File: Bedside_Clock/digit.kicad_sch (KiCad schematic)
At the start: 21 parts

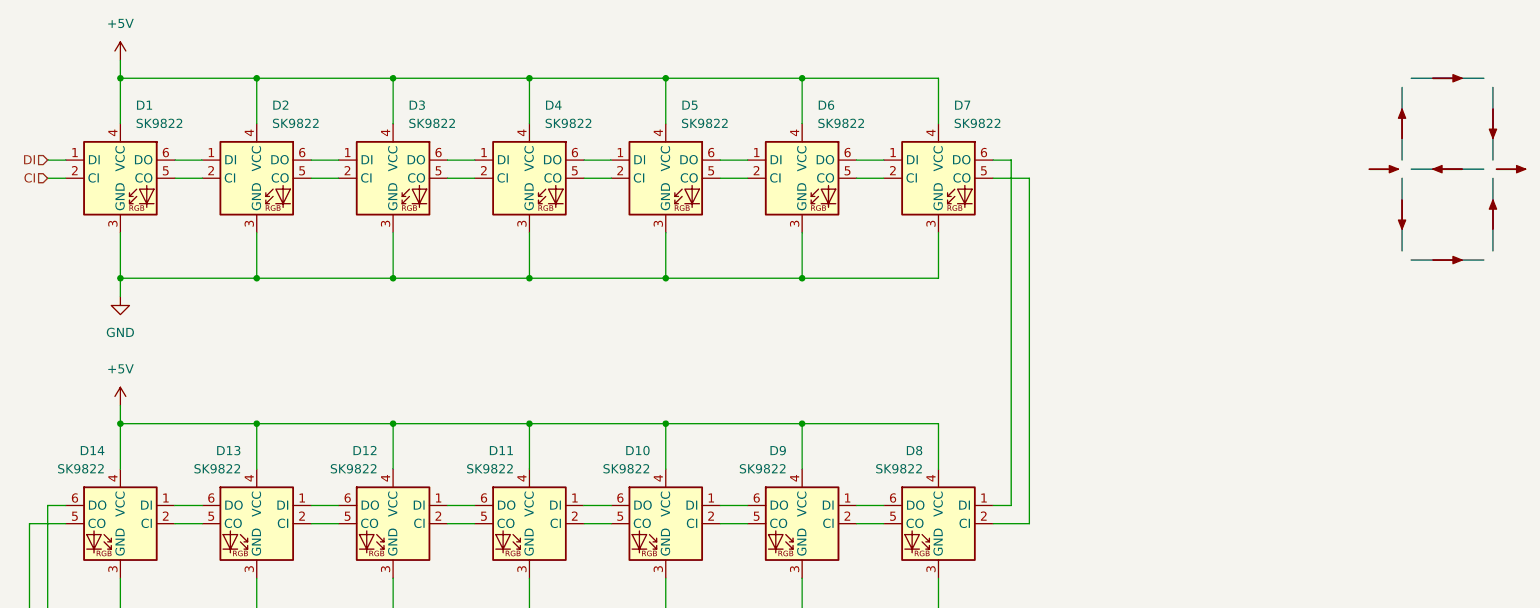
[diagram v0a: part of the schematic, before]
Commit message: [HW] Switch to HD107s (maybe switch to 108s)
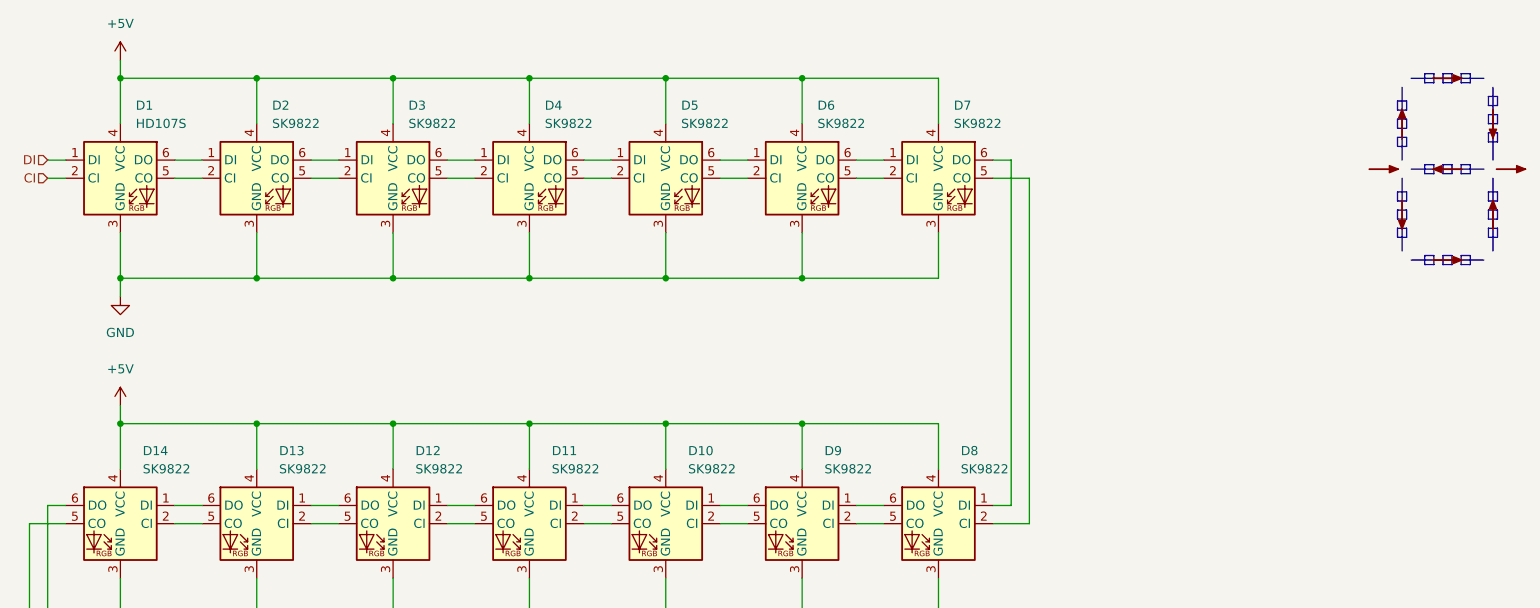
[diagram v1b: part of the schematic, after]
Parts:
- D1: value SK9822 -> HD107S; footprint (none) -> LED_SMD:LED_RGB_5050-6; symbol LED:APA102 -> LED:HD107s; Site (none) -> https://www.ledlightinghut.com/hd107s-5050-rgb-led.html
- D10, D11, D12, D13, D14, D15, D16, D17, D18, D19, D2, D20, D21, D3, D4, D5, D6, D7, D8, D9: footprint (none) -> LED_SMD:LED_RGB_5050-6; symbol LED:APA102 -> LED:HD107s; Site (none) -> https://www.ledlightinghut.com/hd107s-5050-rgb-led.html

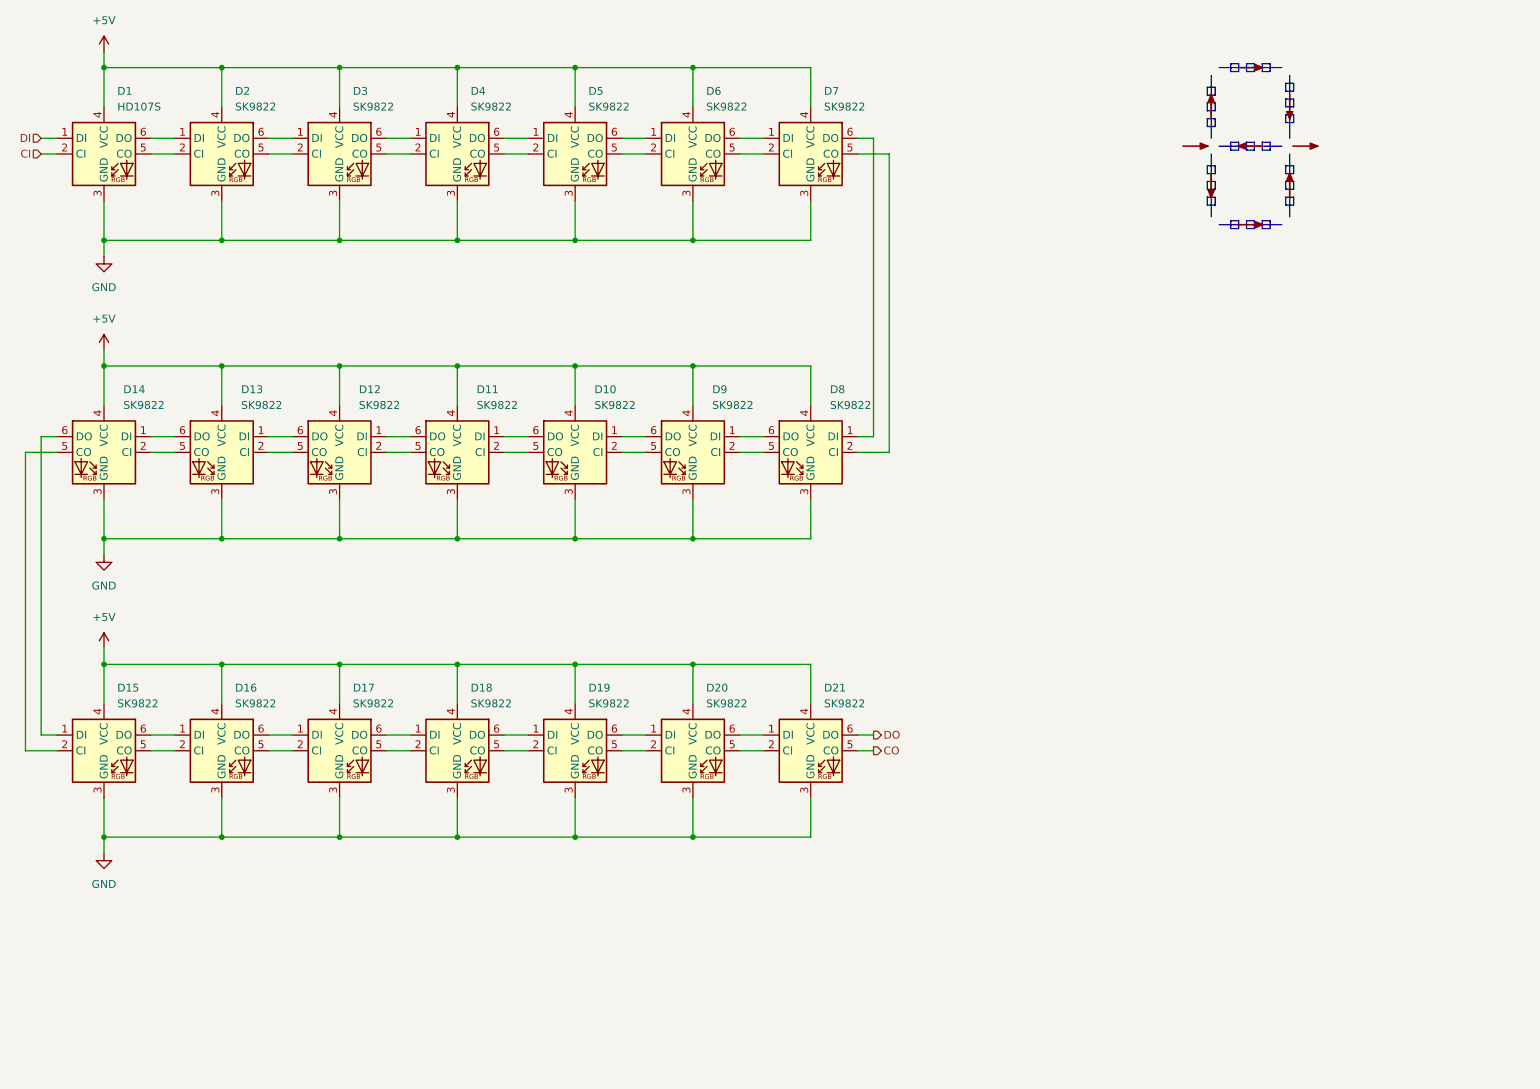
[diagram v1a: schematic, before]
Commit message: [HW] Layout LEDs and first pass add of ESP32 Also add decoupling caps for all LEDs
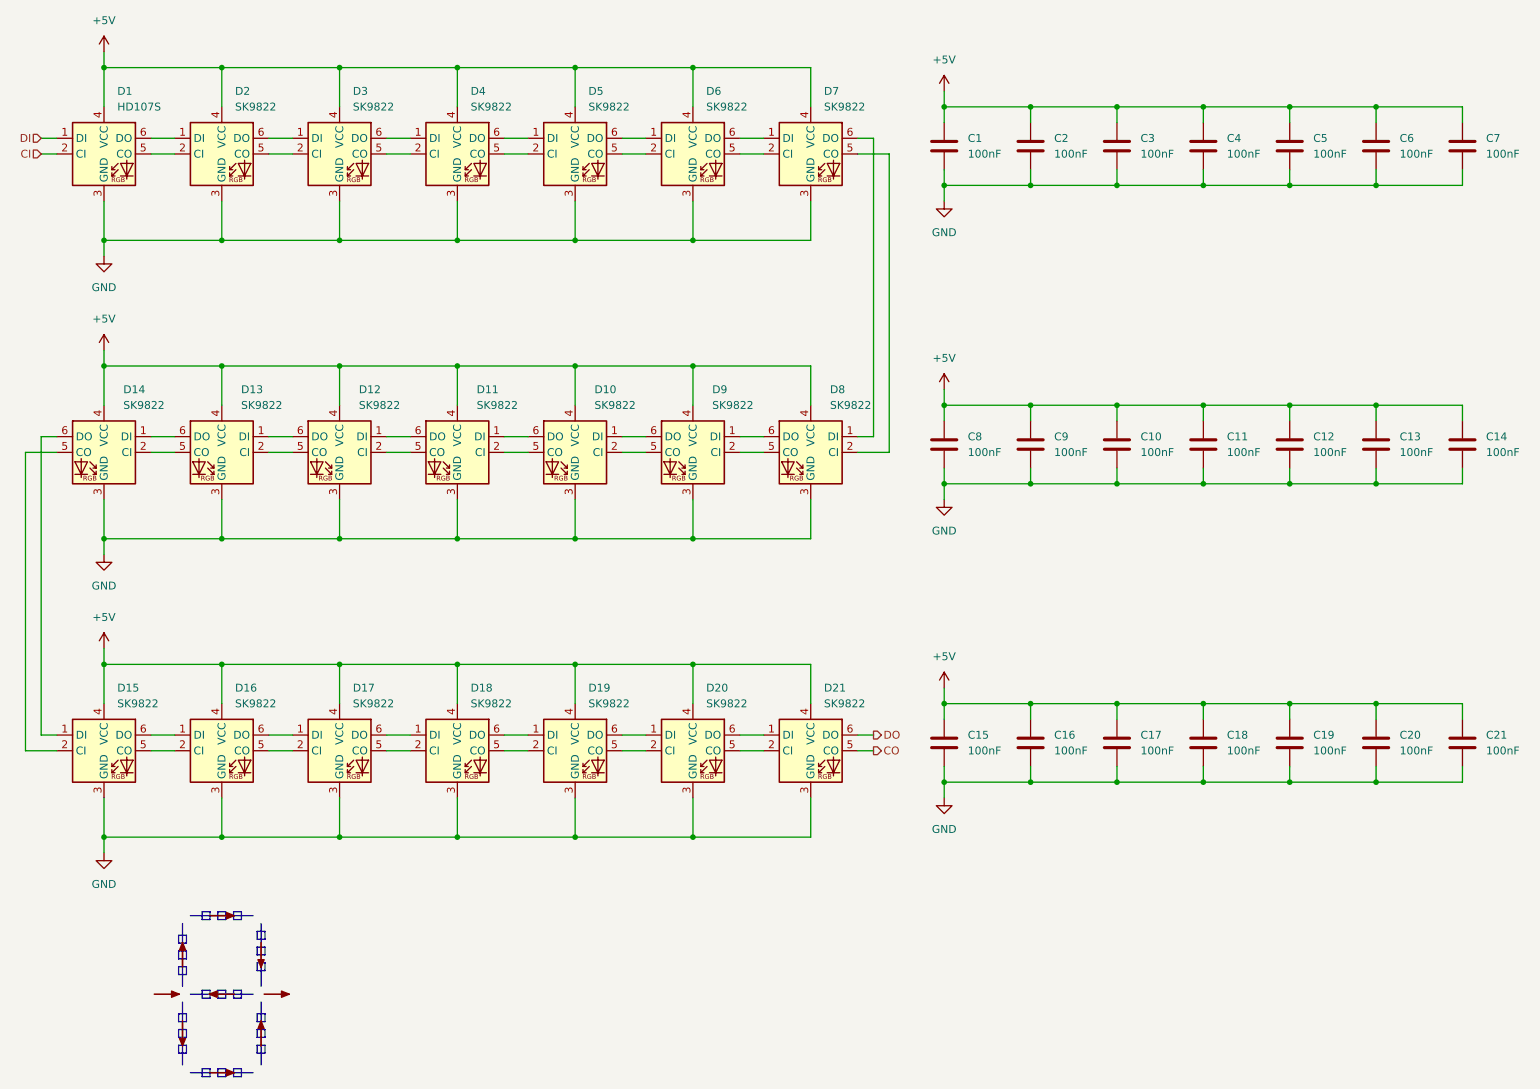
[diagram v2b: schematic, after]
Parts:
- added C1, C10, C11, C12, C13, C14, C15, C16, C17, C18, C19, C2, C20, C21, C3, C4, C5, C6, C7, C8, C9: 100nF, Capacitor_SMD:C_0603_1608Metric, symbol Device:C
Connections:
- net +5V: now also C1.1, C10.1, C11.1, C12.1, C13.1, C14.1, C15.1, C16.1, C17.1, C18.1, C19.1, C2.1, C20.1, C21.1, C3.1, C4.1, C5.1, C6.1, C7.1, C8.1, C9.1
- net GND: now also C1.2, C10.2, C11.2, C12.2, C13.2, C14.2, C15.2, C16.2, C17.2, C18.2, C19.2, C2.2, C20.2, C21.2, C3.2, C4.2, C5.2, C6.2, C7.2, C8.2, C9.2
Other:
- company: (none) -> Matthew Haahr
- title: (none) -> Bedside Clock

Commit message: [HW] Swap component names from SK9822 to HD107S
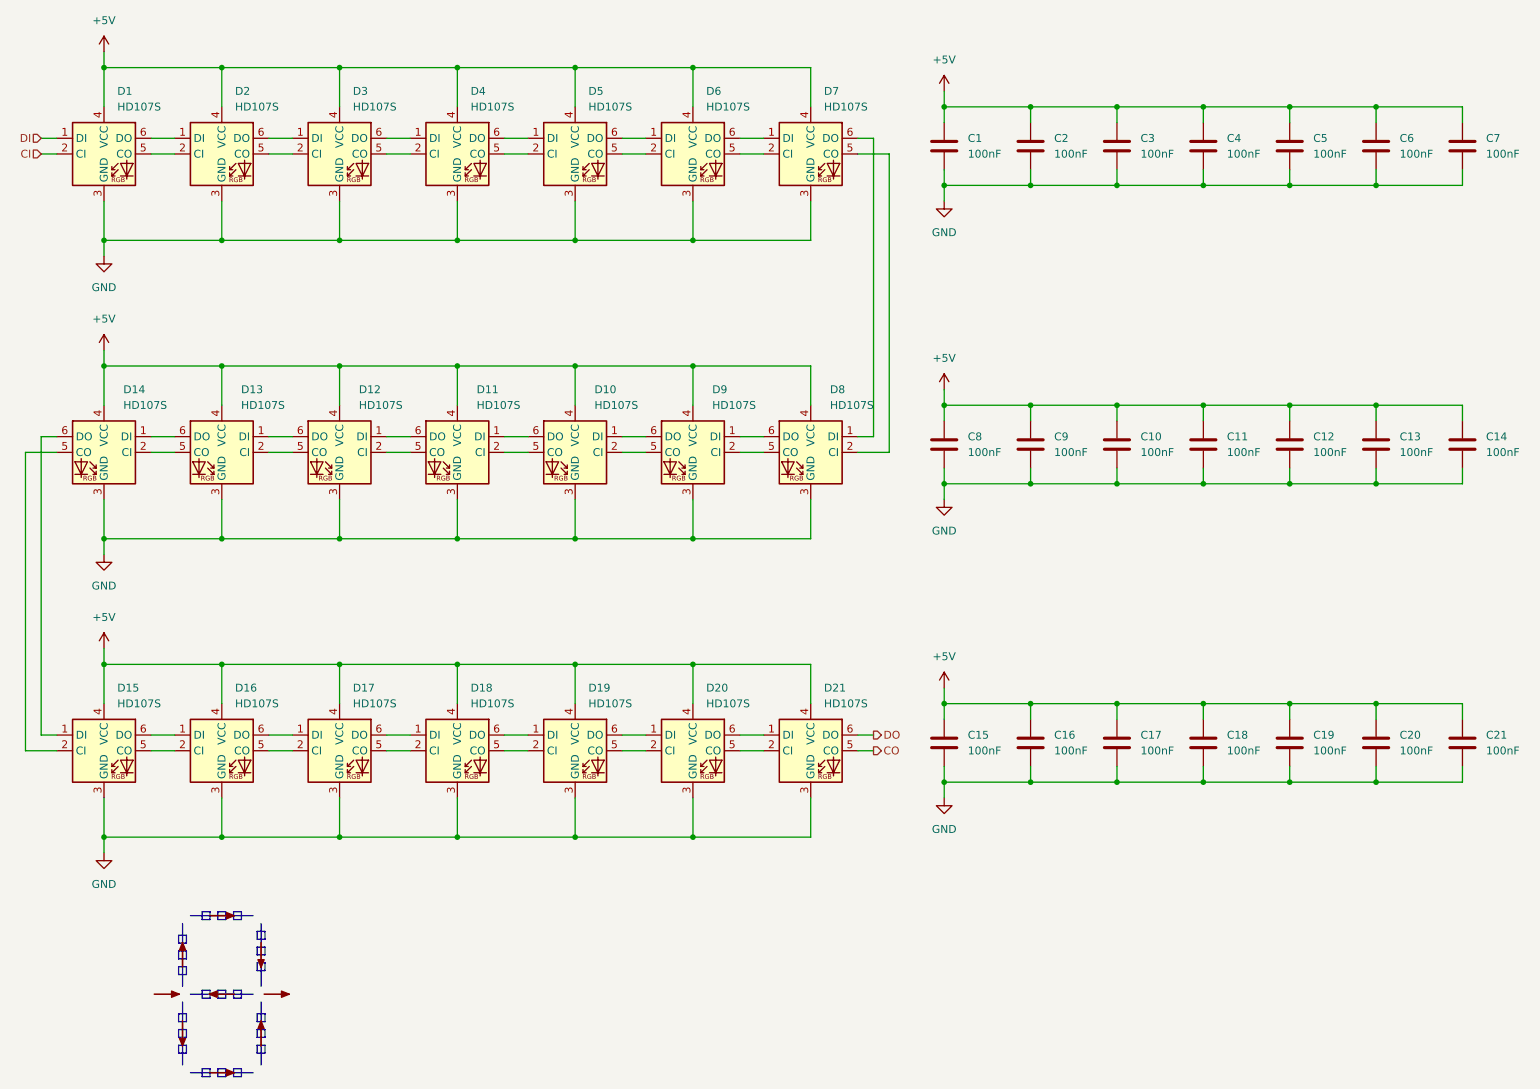
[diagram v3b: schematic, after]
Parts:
- D10, D11, D12, D13, D14, D15, D16, D17, D18, D19, D2, D20, D21, D3, D4, D5, D6, D7, D8, D9: value SK9822 -> HD107S
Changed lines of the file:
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@@
 			)
 		)
-		(property "Value" "SK9822"
+		(property "Value" "HD107S"
 			(at 161.8681 83.82 0)
 			(effects
@@
 			)
 		)
-		(property "Value" "SK9822"
+		(property "Value" "HD107S"
 			(at 84.6933 132.08 0)
 			(effects
@@
 			)
 		)
-		(property "Value" "SK9822"
+		(property "Value" "HD107S"
 			(at 104.7181 83.82 0)
 			(effects
@@
 			)
 		)
-		(property "Value" "SK9822"
+		(property "Value" "HD107S"
 			(at 84.6933 35.56 0)
 			(effects
@@
 			)
 		)
-		(property "Value" "SK9822"
+		(property "Value" "HD107S"
 			(at 122.7933 35.56 0)
 			(effects
@@
 			)
 		)
-		(property "Value" "SK9822"
+		(property "Value" "HD107S"
 			(at 103.7433 132.08 0)
 			(effects
@@
 			)
 		)
-		(property "Value" "SK9822"
+		(property "Value" "HD107S"
 			(at 65.6433 132.08 0)
 			(effects
@@
 			)
 		)
-		(property "Value" "SK9822"
+		(property "Value" "HD107S"
 			(at 141.8433 132.08 0)
 			(effects
@@
 			)
 		)
-		(property "Value" "SK9822"
+		(property "Value" "HD107S"
 			(at 85.6681 83.82 0)
 			(effects
@@
 			)
 		)
-		(property "Value" "SK9822"
+		(property "Value" "HD107S"
 			(at 160.8933 35.56 0)
 			(effects
@@
 			)
 		)
-		(property "Value" "SK9822"
+		(property "Value" "HD107S"
 			(at 46.5933 132.08 0)
 			(effects
@@
 			)
 		)
-		(property "Value" "SK9822"
+		(property "Value" "HD107S"
 			(at 103.7433 35.56 0)
 			(effects
@@
 			)
 		)
-		(property "Value" "SK9822"
+		(property "Value" "HD107S"
 			(at 160.8933 132.08 0)
 			(effects
@@
 			)
 		)
-		(property "Value" "SK9822"
+		(property "Value" "HD107S"
 			(at 66.6181 83.82 0)
 			(effects
@@
 			)
 		)
-		(property "Value" "SK9822"
+		(property "Value" "HD107S"
 			(at 122.7933 132.08 0)
 			(effects
@@
 			)
 		)
-		(property "Value" "SK9822"
+		(property "Value" "HD107S"
 			(at 65.6433 35.56 0)
 			(effects
@@
 			)
 		)
-		(property "Value" "SK9822"
+		(property "Value" "HD107S"
 			(at 47.5681 83.82 0)
 			(effects
@@
 			)
 		)
-		(property "Value" "SK9822"
+		(property "Value" "HD107S"
 			(at 141.8433 35.56 0)
 			(effects
@@
 			)
 		)
-		(property "Value" "SK9822"
+		(property "Value" "HD107S"
 			(at 142.8181 83.82 0)
 			(effects
@@
 			)
 		)
-		(property "Value" "SK9822"
+		(property "Value" "HD107S"
 			(at 123.7681 83.82 0)
 			(effects
